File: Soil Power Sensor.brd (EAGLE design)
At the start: 94 x 67 mm, 62 parts, among them U11 ESP32-C3-MINI-1-N4, U2 INA296A5, U3 THS4532, U4 FSA2466, U5 MAX11201A, U6 REF2033, U7 WIO-E5_MINI, U8 LM27761DSG, U9 MAX9944ASA, X1 Voltage, X2 Current, X3 GND, X4 SDI

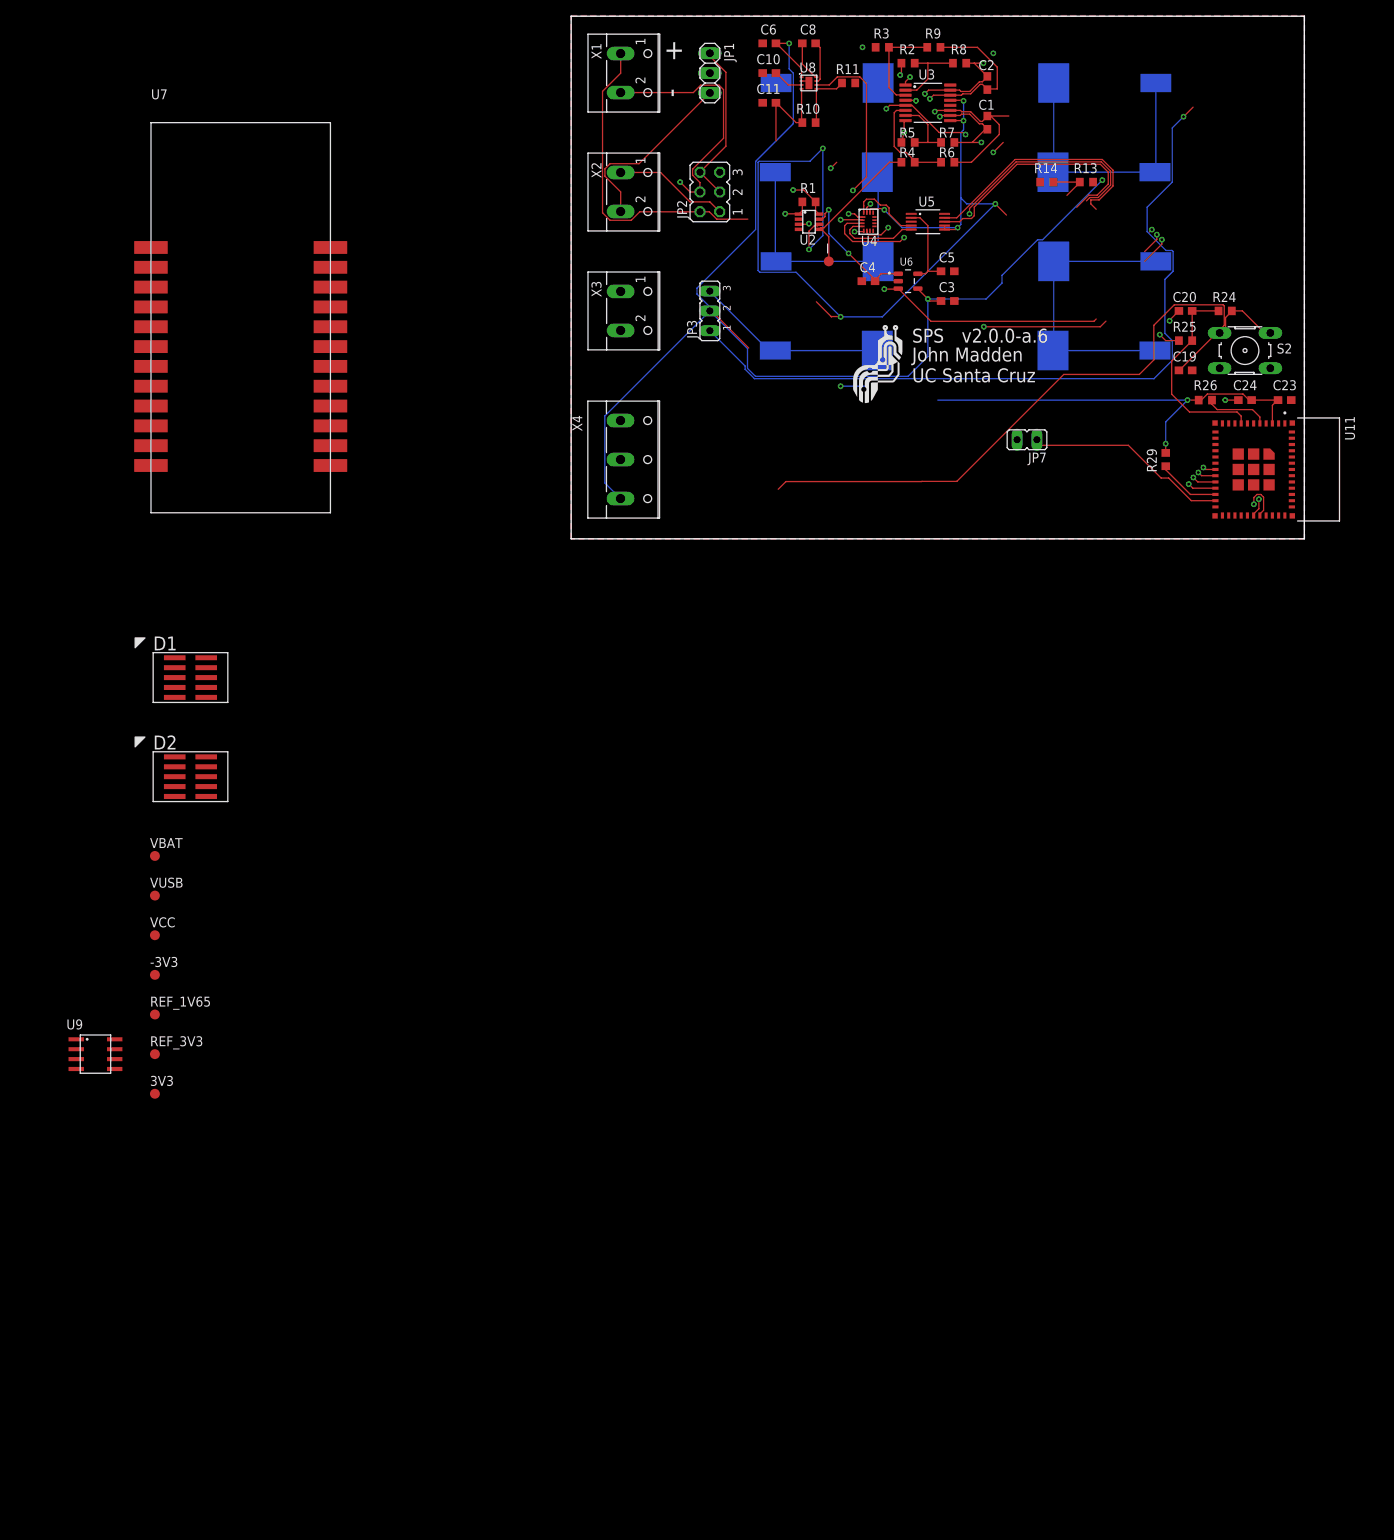
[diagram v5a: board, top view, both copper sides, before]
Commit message: Closes #10
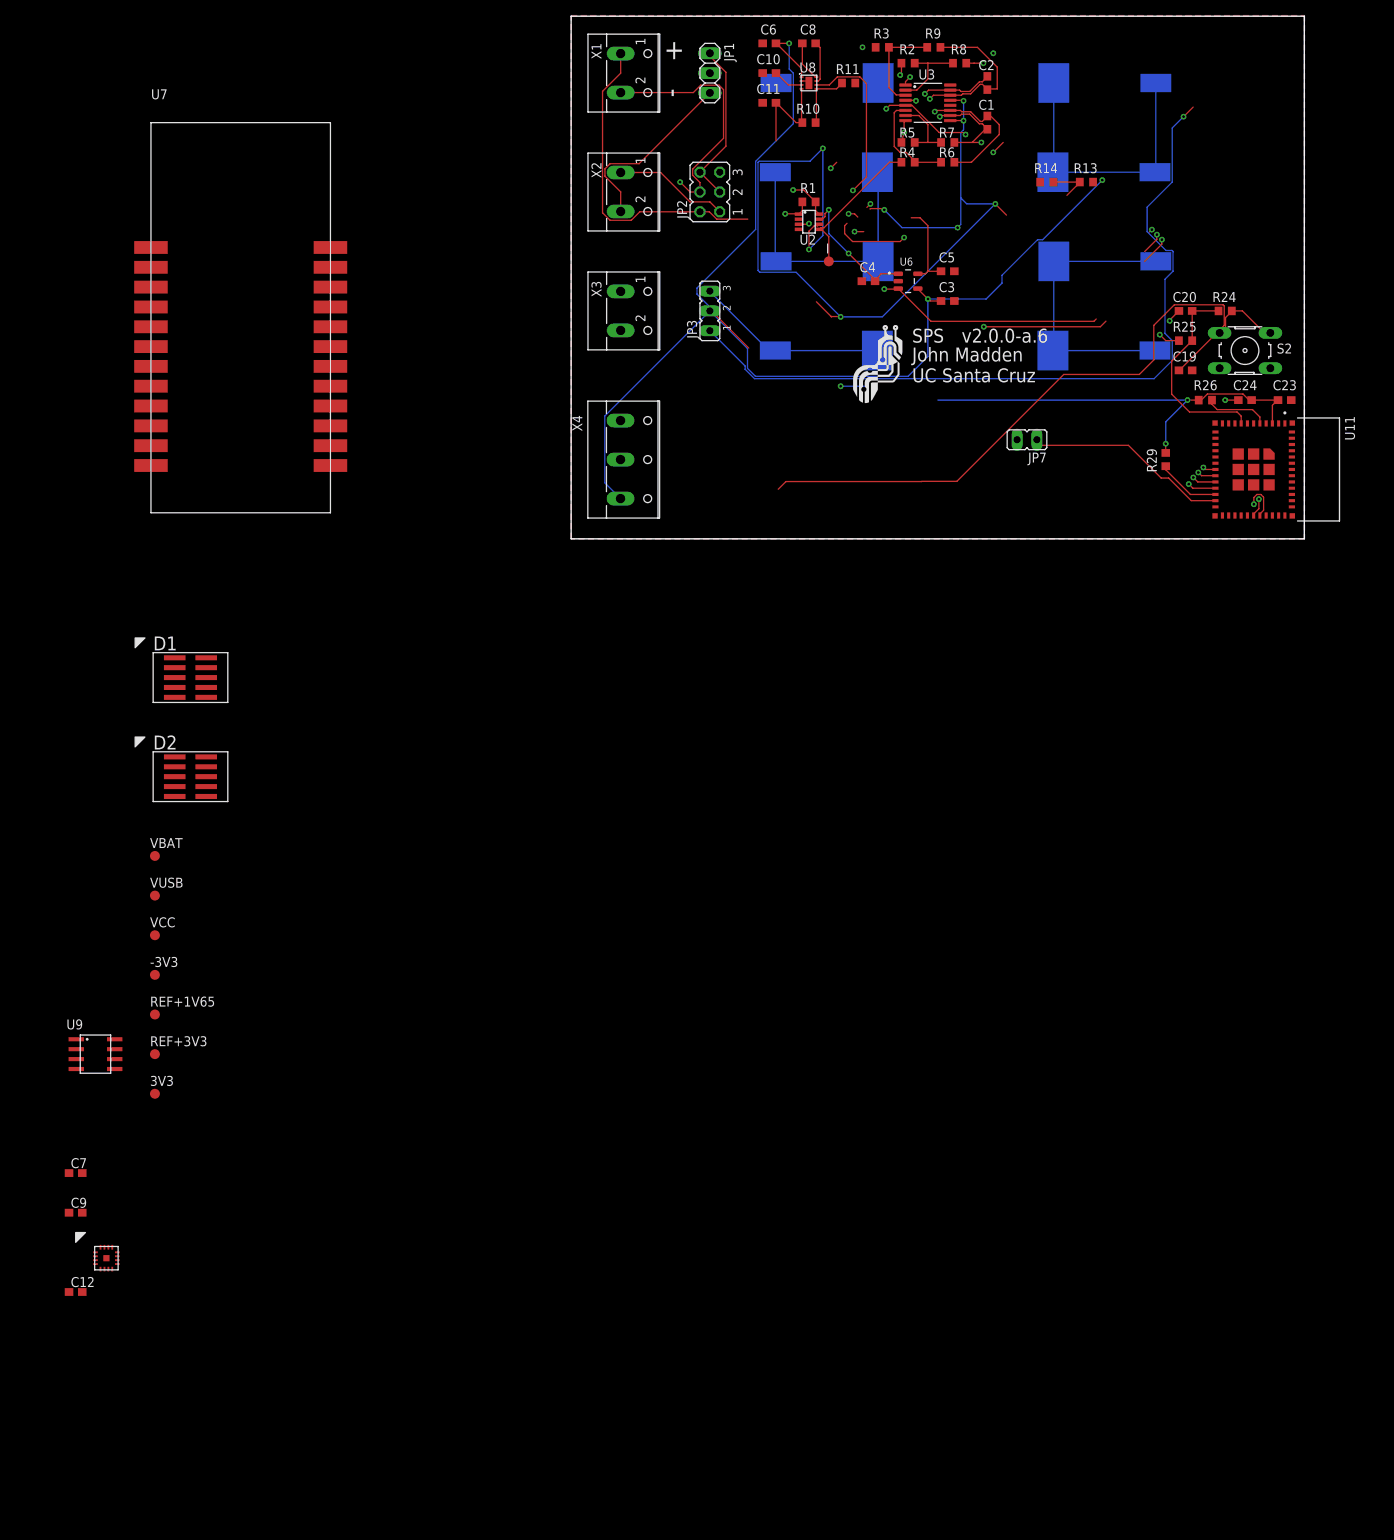
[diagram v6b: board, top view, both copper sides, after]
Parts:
- removed U4: FSA2466, Soil Power Sensor:UQFN40P180X260X50-16N
- removed U5: MAX11201A, Soil Power Sensor:SOP50P490X110-10N
- added C12, C7, C9: 0.1uF, rcl:C0603
- added U1: ADS1219IRTER, Soil Power Sensor:WQFN50P300X300X80-16TPN
- renumbered REF_1V65 to REF+1V65, REF_3V3 to REF+3V3
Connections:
- removed net CURRENT_N: C1.1, R6.2, U3.11, U4.15
- removed net N$41: U4.16, U5.4
- removed net N$42: U4.4, U5.5
- removed net PB13/SPI2_SCK: U5.9
- removed net PB14/SPI2_MISO: U5.8
- removed net PB9/SPI2_NSS: U4.2
- new net ADC_DRDY: U1.12, U7.P10
- new net N$9: C1.1, R6.2, U1.5, U3.11
- new net SCL: U1.14, U7.P1
- new net SDA: U1.13, U7.P2
- net +3V3: now also C7.1, C9.1, U1.1, U1.10, U1.11; no longer U4.14, U5.6, U5.7
- net CURRENT_P: now also U1.4; no longer U4.3
- net GND: now also C12.2, C7.2, C9.2, U1.15, U1.16, U1.2, U1.3, U1.6; no longer U4.6, U5.1, U5.3
- net REF+3V3: now also C12.1, U1.7; no longer U5.2
- net VOLTAGE_N: now also C2.1, U1.9; no longer C2.2, U4.1
- net VOLTAGE_P: now also C2.2, U1.8; no longer C2.1, U4.5
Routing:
- net PB9/SPI2_NSS: track 51.7 -> 0.00 mm, vias 2 -> 0
- net CURRENT_N: track 38.3 -> 0.00 mm, vias 2 -> 0
- net N$9: track 0.00 -> 34.4 mm, vias 0 -> 2
- net PB13/SPI2_SCK: track 32.3 -> 0.00 mm
- net PB14/SPI2_MISO: track 31.9 -> 0.00 mm
- net N$42: track 10.9 -> 0.00 mm
- net N$41: track 9.46 -> 0.00 mm
- net GND: track 8.02 -> 4.50 mm, vias 3 -> 2
- net VOLTAGE_N: track 38.5 -> 35.5 mm
- net +3V3: track 193.1 -> 190.7 mm
- net CURRENT_P: track 46.1 -> 43.8 mm

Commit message: Closes #4
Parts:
- removed C11: 2.2uF, rcl:C0603
- removed R10: 169k, rcl:R0603
- removed R11: 100k, rcl:R0603
- removed U8: LM27761DSG, Soil Power Sensor:SON50P200X200X80-9TPN
- added U4: TPS60400DBV, Soil Power Sensor:SOT95P280X145-5N
- C10, C6: value 4.7uF -> 1uF
- moved C8 196.9 mm to (-68.6, -106.7), turned to 0 degrees
- moved C10 195.5 mm to (-68.6, -111.8), turned to 0 degrees
- moved C6 190.0 mm to (-68.6, -101.6), turned to 0 degrees
- moved -3V3 62.8 mm to (-68.6, -116.8)
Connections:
- removed net N$32: C8.1, U8.7
- removed net N$44: R10.1, R11.2, U8.5
- removed net N$5: C8.2, U8.8
- removed net N$53: C10.1, U8.3
- new net N$10: C6.2, U4.3
- new net N$7: C6.1, U4.5
- net +3V3: now also C10.1, U4.2
- net -3V3: now also C8.1, U4.1; no longer C11.1, R10.2, U8.4
- net GND: now also C8.2, U4.4; no longer C11.2, C6.2, R11.1, U8.2, U8.9
- net PC1: no longer U8.6
- net VCC: no longer C6.1, U8.1
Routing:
- net -3V3: track 13.7 -> 0.00 mm
- net N$44: track 7.99 -> 0.00 mm
- net VCC: track 160.0 -> 152.6 mm
- net N$32: track 5.43 -> 0.00 mm
- net N$5: track 5.15 -> 0.00 mm
- net N$53: track 3.91 -> 0.00 mm
- net PC1: track 69.0 -> 67.3 mm
- net GND: track 4.50 -> 3.45 mm

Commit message: Closes #9
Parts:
- added U5: FM24CL16B-G, Soil Power Sensor:SOIC127P602X164-8N
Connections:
- net +3V3: now also U5.P8
- net GND: now also U5.P4
- net SCL: now also U5.P6
- net SDA: now also U5.P5
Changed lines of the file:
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@@
 <attribute name="VALUE" x="-69.215" y="-117.602" size="0.0254" layer="27"/>
+</element>
+<element name="U5" library="Soil Power Sensor" package="SOIC127P602X164-8N" value="FM24CL16B-G" x="-68.58" y="-121.92" smashed="yes">
+<attribute name="AUTHOR" value="John Madden &lt;jmadden173@pm.me&gt;" x="-68.58" y="-121.92" size="1.778" layer="27" display="off"/>
+<attribute name="DATE_CREATED" value="2023-09-11" x="-68.58" y="-121.92" size="1.778" layer="27" display="off"/>
+<attribute name="DATE_MODIFIED" value="2023-09-11" x="-68.58" y="-121.92" size="1.778" layer="27" display="off"/>
+<attribute name="MFC" value="Cypress" x="-68.58" y="-121.92" size="1.778" layer="27" display="off"/>
+<attribute name="MPN" value="FM24CL16B-G" x="-68.58" y="-121.92" size="1.778" layer="27" display="off"/>
+<attribute name="NAME" x="-69.48" y="-121.12366875" size="1.778" layer="25"/>
+<attribute name="VALUE" x="-69.48" y="-128.30433125" size="1.778" layer="27"/>
 </element>
 </elements>
@@
 <contactref element="C10" pad="1"/>
 <contactref element="U4" pad="2"/>
+<contactref element="U5" pad="P8"/>
+<wire x1="-69.43" y1="-111.76" x2="-62.58" y2="-121.92" width="0" layer="19" extent="1-1"/>
 <wire x1="-69.835" y1="-93.98" x2="-69.43" y2="-111.76" width="0" layer="19" extent="1-1"/>
 <wire x1="-60.96" y1="-91.44" x2="-69.835" y2="-93.98" width="0" layer="19" extent="1-1"/>
@@
 <contactref element="C8" pad="2"/>
 <contactref element="C10" pad="2"/>
+<contactref element="U5" pad="P4"/>
+<wire x1="-67.73" y1="-111.76" x2="-68.58" y2="-125.73" width="0" layer="19" extent="1-1"/>
 <wire x1="-67.73" y1="-106.68" x2="-67.73" y2="-111.76" width="0" layer="19" extent="1-1"/>
 <wire x1="-62.65" y1="-96.52" x2="-67.73" y2="-106.68" width="0" layer="19" extent="1-1"/>
@@
 <contactref element="U7" pad="P1"/>
 <contactref element="U1" pad="14"/>
+<contactref element="U5" pad="P6"/>
+<wire x1="-59.31" y1="-90.79" x2="-62.58" y2="-124.46" width="0" layer="19" extent="1-1"/>
 <wire x1="-53.848" y1="34.798" x2="-59.31" y2="-90.79" width="0" layer="19" extent="1-1"/>
 </signal>
@@
 <contactref element="U7" pad="P2"/>
 <contactref element="U1" pad="13"/>
+<contactref element="U5" pad="P5"/>
+<wire x1="-58.81" y1="-90.79" x2="-62.58" y2="-125.73" width="0" layer="19" extent="1-1"/>
 <wire x1="-53.848" y1="32.258" x2="-58.81" y2="-90.79" width="0" layer="19" extent="1-1"/>
 </signal>
